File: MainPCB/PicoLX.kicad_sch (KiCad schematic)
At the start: 82 parts, among them J1 USB_C_Receptacle_USB2.0, J2 Conn_01x03, SW1 SW_Push, U1 RP2040, U2 W25Q32JVSS, U3 NCP1117-3.3_SOT223, U4 SN74LV1T34DBV, Y1 12.000MHz

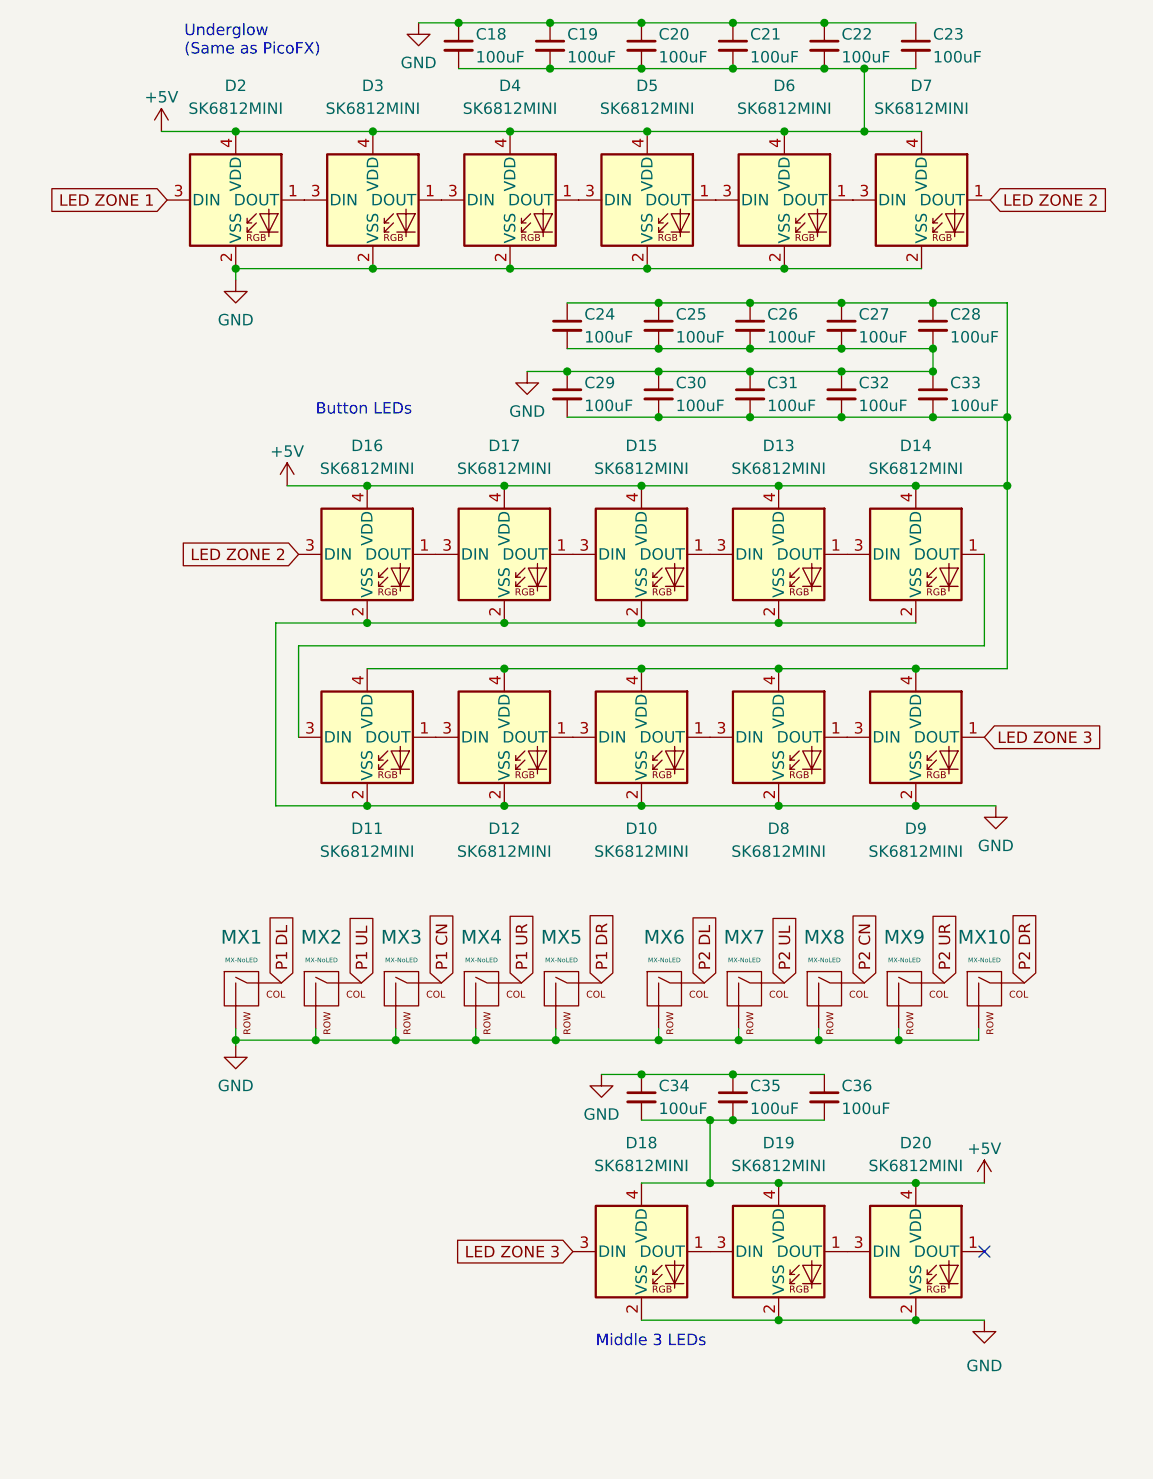
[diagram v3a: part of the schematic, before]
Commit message: fancy plate graphics, reroute all the LEDs because wrong pinout
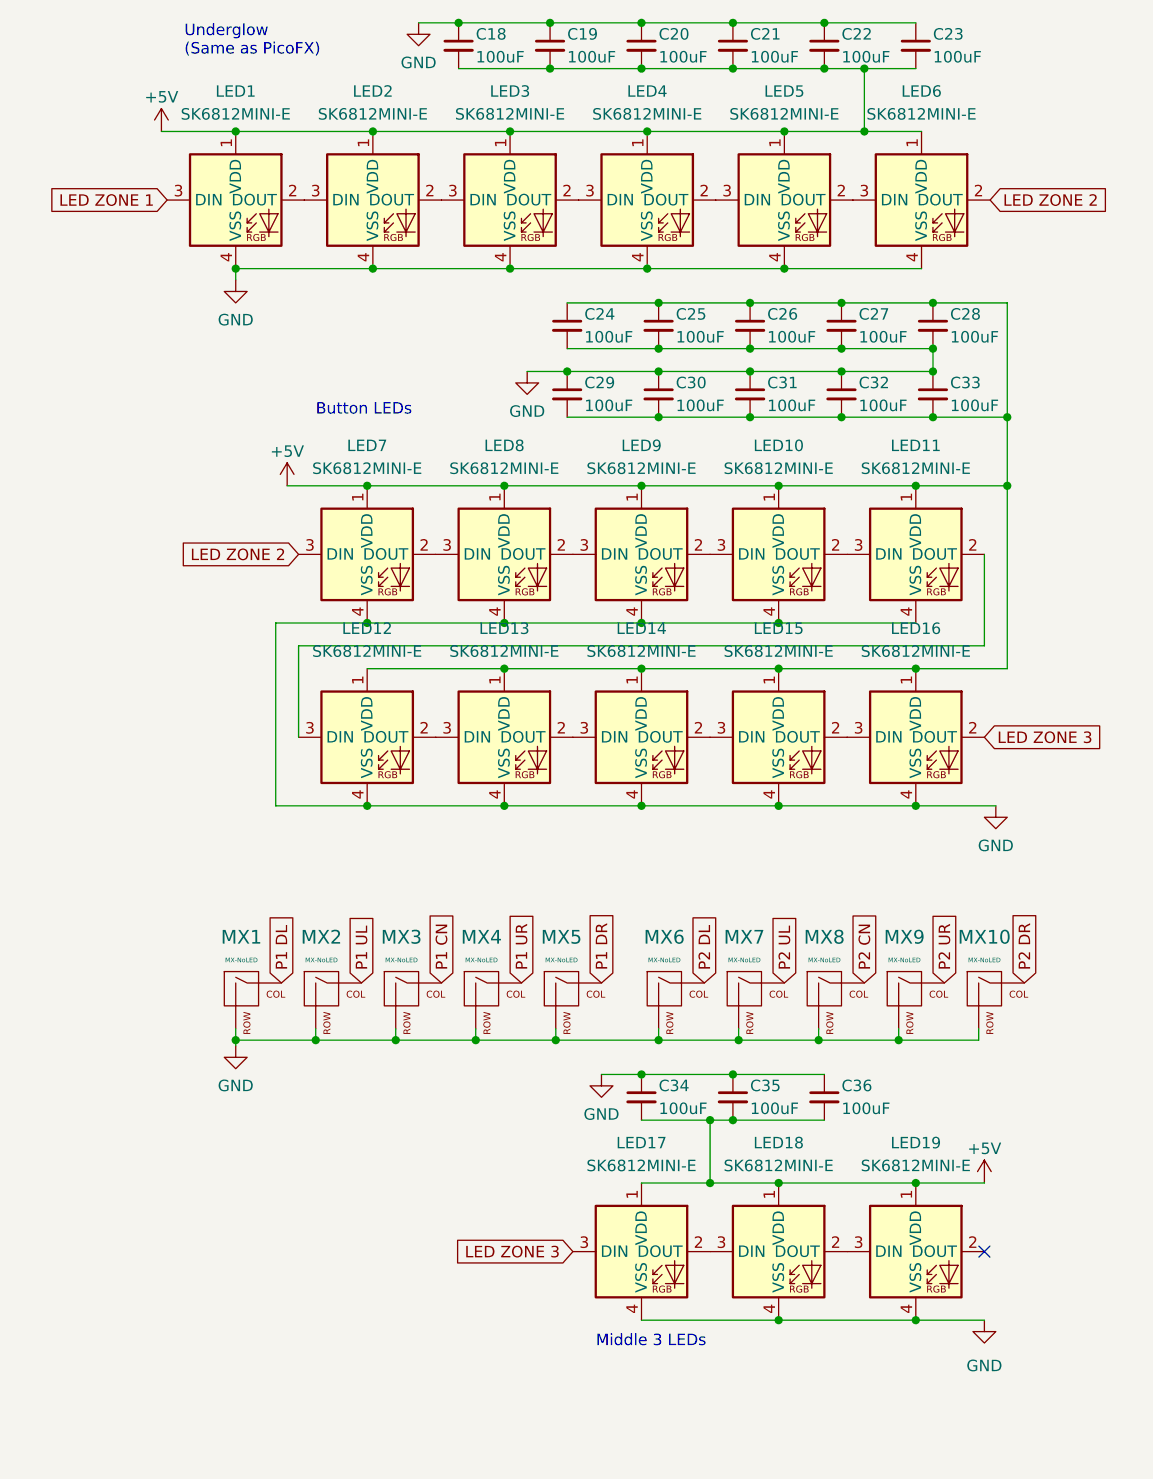
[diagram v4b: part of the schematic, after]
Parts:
- removed D10, D11, D12, D13, D14, D15, D16, D17, D18, D19, D2, D20, D3, D4, D5, D6, D7, D8, D9: SK6812MINI, marbastlib-various:LED_6028R, symbol LED:SK6812MINI
- added LED1, LED10, LED11, LED12, LED13, LED14, LED15, LED16, LED17, LED18, LED19, LED2, LED3, LED4, LED5, LED6, LED7, LED8, LED9: SK6812MINI-E, marbastlib-various:LED_6028R, symbol marbastlib-various:SK6812MINI-E
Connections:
- net +5V: now also LED1.1 (VDD), LED10.1 (VDD), LED11.1 (VDD), LED12.1 (VDD), LED13.1 (VDD), LED14.1 (VDD), LED15.1 (VDD), LED16.1 (VDD), LED17.1 (VDD), LED18.1 (VDD), LED19.1 (VDD), LED2.1 (VDD), LED3.1 (VDD), LED4.1 (VDD), LED5.1 (VDD), LED6.1 (VDD), LED7.1 (VDD), LED8.1 (VDD), LED9.1 (VDD)
- net GND: now also LED1.4 (VSS), LED10.4 (VSS), LED11.4 (VSS), LED12.4 (VSS), LED13.4 (VSS), LED14.4 (VSS), LED15.4 (VSS), LED16.4 (VSS), LED17.4 (VSS), LED18.4 (VSS), LED19.4 (VSS), LED2.4 (VSS), LED3.4 (VSS), LED4.4 (VSS), LED5.4 (VSS), LED6.4 (VSS), LED7.4 (VSS), LED8.4 (VSS), LED9.4 (VSS)
- net LED ZONE 1: now also LED1.3 (DIN)
- net LED ZONE 2: now also LED6.2 (DOUT), LED7.3 (DIN)
- net LED ZONE 3: now also LED16.2 (DOUT), LED17.3 (DIN)
- new net: LED5.2 (DOUT), LED6.3 (DIN)
- new net: LED11.2 (DOUT), LED12.3 (DIN)
- new net: LED10.2 (DOUT), LED11.3 (DIN)
- new net: LED18.2 (DOUT), LED19.3 (DIN)
- new net: LED4.2 (DOUT), LED5.3 (DIN)
- new net: LED15.2 (DOUT), LED16.3 (DIN)
- new net: LED14.2 (DOUT), LED15.3 (DIN)
- new net: LED2.2 (DOUT), LED3.3 (DIN)
- new net: LED1.2 (DOUT), LED2.3 (DIN)
- new net: LED17.2 (DOUT), LED18.3 (DIN)
- new net: LED13.2 (DOUT), LED14.3 (DIN)
- new net: LED3.2 (DOUT), LED4.3 (DIN)
- new net: LED7.2 (DOUT), LED8.3 (DIN)
- new net: LED10.3 (DIN), LED9.2 (DOUT)
- new net: LED8.2 (DOUT), LED9.3 (DIN)
- new net: LED12.2 (DOUT), LED13.3 (DIN)

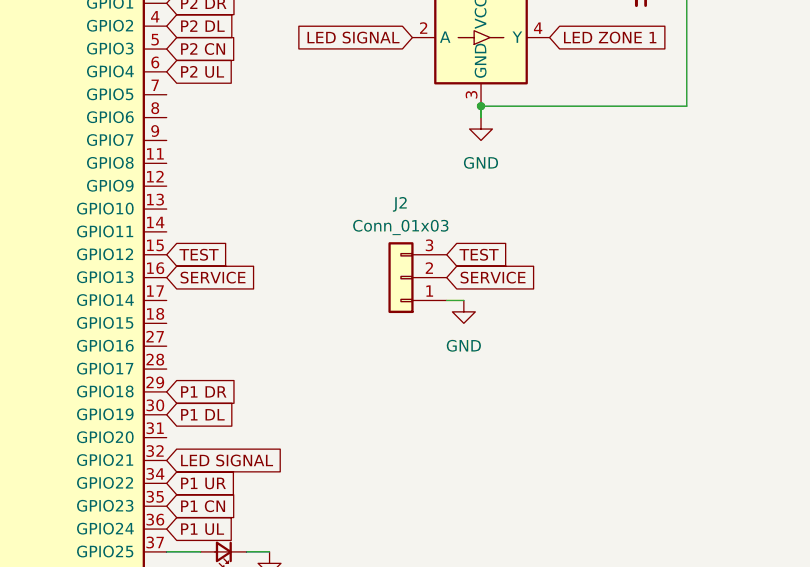
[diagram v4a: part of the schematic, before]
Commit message: Move buttons, add totally 100% real LEDs to plate
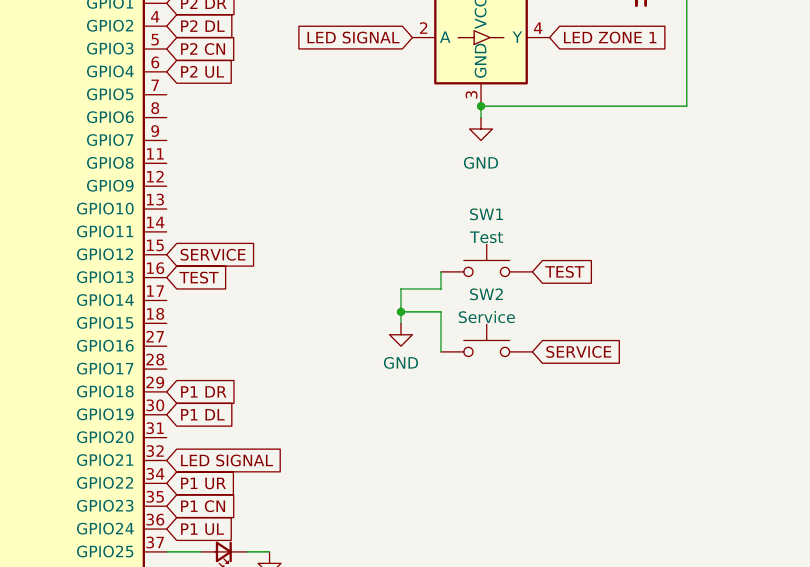
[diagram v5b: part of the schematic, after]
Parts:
- removed J2: Conn_01x03, Connector_PinHeader_2.54mm:PinHeader_1x03_P2.54mm_Vertical, symbol Connector_Generic:Conn_01x03
- added SW1: Test, Button_Switch_THT:SW_Tactile_SPST_Angled_PTS645Vx39-2LFS, symbol Switch:SW_Push
- added SW2: Service, Button_Switch_THT:SW_Tactile_SPST_Angled_PTS645Vx39-2LFS, symbol Switch:SW_Push
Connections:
- net GND: now also SW1.1, SW2.1
- net SERVICE: now also U1.15 (GPIO12), SW2.2; no longer U1.16 (GPIO13)
- net TEST: now also U1.16 (GPIO13), SW1.2; no longer U1.15 (GPIO12)
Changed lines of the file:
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@@
   (junction (at 243.205 50.165) (diameter 0) (color 0 0 0 0)
   )
+  (junction (at 118.11 96.52) (diameter 0) (color 0 0 0 0)
+  )
   (junction (at 109.22 41.91) (diameter 0) (color 0 0 0 0)
   )
@@
     (stroke (width 0) (type default))
   )
+  (wire (pts (xy 122.555 100.965) (xy 122.555 96.52))
+    (stroke (width 0) (type default))
+  )
   (wire (pts (xy 69.85 178.435) (xy 71.755 178.435))
     (stroke (width 0) (type default))
@@
     (stroke (width 0) (type default))
   )
+  (wire (pts (xy 122.555 93.98) (xy 122.555 92.075))
+    (stroke (width 0) (type default))
+  )
   (wire (pts (xy 238.76 135.89) (xy 238.76 142.875))
     (stroke (width 0) (type default))
@@
     (stroke (width 0) (type default))
   )
+  (wire (pts (xy 118.11 96.52) (xy 118.11 97.79))
+    (stroke (width 0) (type default))
+  )
   (wire (pts (xy 56.515 41.91) (xy 56.515 36.83))
     (stroke (width 0) (type default))
@@
     (stroke (width 0) (type default))
   )
+  (wire (pts (xy 118.11 93.98) (xy 118.11 96.52))
+    (stroke (width 0) (type default))
+  )
   (wire (pts (xy 201.295 41.275) (xy 216.535 41.275))
     (stroke (width 0) (type default))
@@
     (stroke (width 0) (type default))
   )
+  (wire (pts (xy 122.555 96.52) (xy 118.11 96.52))
+    (stroke (width 0) (type default))
+  )
   (wire (pts (xy 121.285 25.4) (xy 111.125 25.4))
     (stroke (width 0) (type default))
@@
     (stroke (width 0) (type default))
   )
-  (wire (pts (xy 123.19 95.25) (xy 125.095 95.25))
-    (stroke (width 0) (type default))
-  )
   (wire (pts (xy 76.835 20.32) (xy 80.645 20.32))
     (stroke (width 0) (type default))
@@
     (stroke (width 0) (type default))
   )
+  (wire (pts (xy 118.11 93.98) (xy 122.555 93.98))
+    (stroke (width 0) (type default))
+  )
   (wire (pts (xy 243.205 50.165) (xy 253.365 50.165))
     (stroke (width 0) (type default))
@@
     )
   )
-  (global_label "SERVICE" (shape input) (at 92.075 92.71 0) (fields_autoplaced)
+  (global_label "SERVICE" (shape input) (at 92.075 90.17 0) (fields_autoplaced)
     (effects (font (size 1.27 1.27)) (justify left))
-    (property "Intersheetrefs" "${INTERSHEET_REFS}" (at 102.7217 92.71 0)
+    (property "Intersheetrefs" "${INTERSHEET_REFS}" (at 102.7217 90.17 0)
       (effects (font (size 1.27 1.27)) (justify left) hide)
     )
@@
     )
   )
-  (global_label "TEST" (shape input) (at 92.075 90.17 0) (fields_autoplaced)
+  (global_label "TEST" (shape input) (at 92.075 92.71 0) (fields_autoplaced)
     (effects (font (size 1.27 1.27)) (justify left))
-    (property "Intersheetrefs" "${INTERSHEET_REFS}" (at 99.2745 90.17 0)
+    (property "Intersheetrefs" "${INTERSHEET_REFS}" (at 99.2745 92.71 0)
       (effects (font (size 1.27 1.27)) (justify left) hide)
     )
@@
     )
   )
-  (global_label "TEST" (shape input) (at 123.19 90.17 0) (fields_autoplaced)
+  (global_label "TEST" (shape input) (at 132.715 92.075 0) (fields_autoplaced)
     (effects (font (size 1.27 1.27)) (justify left))
-    (property "Intersheetrefs" "${INTERSHEET_REFS}" (at 130.3895 90.17 0)
+    (property "Intersheetrefs" "${INTERSHEET_REFS}" (at 139.9145 92.075 0)
       (effects (font (size 1.27 1.27)) (justify left) hide)
     )
@@
     )
   )
-  (global_label "SERVICE" (shape input) (at 123.19 92.71 0) (fields_autoplaced)
+  (global_label "SERVICE" (shape input) (at 132.715 100.965 0) (fields_autoplaced)
     (effects (font (size 1.27 1.27)) (justify left))
-    (property "Intersheetrefs" "${INTERSHEET_REFS}" (at 133.8367 92.71 0)
+    (property "Intersheetrefs" "${INTERSHEET_REFS}" (at 143.3617 100.965 0)
       (effects (font (size 1.27 1.27)) (justify left) hide)
     )
@@
     )
   )
-  (symbol (lib_id "Connector_Generic:Conn_01x03") (at 118.11 92.71 180) (unit 1)
-    (in_bom yes) (on_board yes) (dnp no) (fields_autoplaced)
-    (property "Reference" "J2" (at 118.11 84.455 0)
-      (effects (font (size 1.27 1.27)))
-    )
-    (property "Value" "Conn_01x03" (at 118.11 86.995 0)
-      (effects (font (size 1.27 1.27)))
-    )
-    (property "Footprint" "Connector_PinHeader_2.54mm:PinHeader_1x03_P2.54mm_Vertical" (at 118.11 92.71 0)
-      (effects (font (size 1.27 1.27)) hide)
-    )
-    (property "Datasheet" "~" (at 118.11 92.71 0)
-      (effects (font (size 1.27 1.27)) hide)
-    )
-    (pin "1")
-    (pin "2")
-    (pin "3")
-    (instances
-      (project "PicoLX"
-        (path "/c5e5d8b8-bebd-4318-85a6-adbafb95dd10"
-          (reference "J2") (unit 1)
-        )
-      )
-    )
-  )
   (symbol (lib_id "Device:C_Small") (at 251.46 16.51 0) (unit 1)
     (in_bom yes) (on_board yes) (dnp no)
@@
     )
   )
+  (symbol (lib_id "Switch:SW_Push") (at 127.635 92.075 0) (unit 1)
+    (in_bom yes) (on_board yes) (dnp no) (fields_autoplaced)
+    (property "Reference" "SW1" (at 127.635 85.725 0)
+      (effects (font (size 1.27 1.27)))
+    )
+    (property "Value" "Test" (at 127.635 88.265 0)
+      (effects (font (size 1.27 1.27)))
+    )
+    (property "Footprint" "Button_Switch_THT:SW_Tactile_SPST_Angled_PTS645Vx39-2LFS" (at 127.635 86.995 0)
+      (effects (font (size 1.27 1.27)) hide)
+    )
+    (property "Datasheet" "~" (at 127.635 86.995 0)
+      (effects (font (size 1.27 1.27)) hide)
+    )
+    (pin "1")
+    (pin "2")
+    (instances
+      (project "MainPlate"
+        (path "/99dc8099-532a-4f61-b2bb-5f32226d143c"
+          (reference "SW1") (unit 1)
+        )
+      )
+      (project "PicoLX"
+        (path "/c5e5d8b8-bebd-4318-85a6-adbafb95dd10"
+          (reference "SW2") (unit 1)
+        )
+      )
+    )
+  )
   (symbol (lib_id "marbastlib-various:SK6812MINI-E") (at 201.295 33.655 0) (unit 1)
     (in_bom yes) (on_board yes) (dnp no)
@@
     )
   )
-  (symbol (lib_id "power:GND") (at 125.095 95.25 0) (unit 1)
-    (in_bom yes) (on_board yes) (dnp no) (fields_autoplaced)
-    (property "Reference" "#PWR034" (at 125.095 101.6 0)
-      (effects (font (size 1.27 1.27)) hide)
-    )
-    (property "Value" "GND" (at 125.095 100.33 0)
-      (effects (font (size 1.27 1.27)))
-    )
-    (property "Footprint" "" (at 125.095 95.25 0)
-      (effects (font (size 1.27 1.27)) hide)
-    )
-    (property "Datasheet" "" (at 125.095 95.25 0)
-      (effects (font (size 1.27 1.27)) hide)
-    )
-    (pin "1")
-    (instances
-      (project "PicoLX"
-        (path "/c5e5d8b8-bebd-4318-85a6-adbafb95dd10"
-          (reference "#PWR034") (unit 1)
-        )
-      )
-      (project "Panel"
-        (path "/f55927e3-6490-4e79-9229-dceeb24f0064"
-          (reference "#PWR015") (unit 1)
-        )
-      )
-    )
-  )
   (symbol (lib_name "GND_1") (lib_id "power:GND") (at 186.055 42.545 0) (unit 1)
     (in_bom yes) (on_board yes) (dnp no) (fields_autoplaced)
@@
     )
   )
+  (symbol (lib_id "Switch:SW_Push") (at 127.635 100.965 0) (unit 1)
+    (in_bom yes) (on_board yes) (dnp no) (fields_autoplaced)
+    (property "Reference" "SW2" (at 127.635 94.615 0)
+      (effects (font (size 1.27 1.27)))
+    )
+    (property "Value" "Service" (at 127.635 97.155 0)
+      (effects (font (size 1.27 1.27)))
+    )
+    (property "Footprint" "Button_Switch_THT:SW_Tactile_SPST_Angled_PTS645Vx39-2LFS" (at 127.635 95.885 0)
+      (effects (font (size 1.27 1.27)) hide)
+    )
+    (property "Datasheet" "~" (at 127.635 95.885 0)
+      (effects (font (size 1.27 1.27)) hide)
+    )
+    (pin "1")
+    (pin "2")
+    (instances
+      (project "MainPlate"
+        (path "/99dc8099-532a-4f61-b2bb-5f32226d143c"
+          (reference "SW2") (unit 1)
+        )
+      )
+      (project "PicoLX"
+        (path "/c5e5d8b8-bebd-4318-85a6-adbafb95dd10"
+          (reference "SW3") (unit 1)
+        )
+      )
+    )
+  )
   (symbol (lib_id "marbastlib-various:SK6812MINI-E") (at 216.535 33.655 0) (unit 1)
     (in_bom yes) (on_board yes) (dnp no)
@@
         )
       )
+    )
+  )
+  (symbol (lib_id "power:GND") (at 118.11 97.79 0) (unit 1)
+    (in_bom yes) (on_board yes) (dnp no) (fields_autoplaced)
+    (property "Reference" "#PWR01" (at 118.11 104.14 0)
+      (effects (font (size 1.27 1.27)) hide)
+    )
+    (property "Value" "GND" (at 118.11 102.235 0)
+      (effects (font (size 1.27 1.27)))
+    )
+    (property "Footprint" "" (at 118.11 97.79 0)
+      (effects (font (size 1.27 1.27)) hide)
+    )
+    (property "Datasheet" "" (at 118.11 97.79 0)
+      (effects (font (size 1.27 1.27)) hide)
+    )
+    (pin "1")
+    (instances
+      (project "MainPlate"
+        (path "/99dc8099-532a-4f61-b2bb-5f32226d143c"
+          (reference "#PWR01") (unit 1)
+        )
+      )
+      (project "PicoLX"
+        (path "/c5e5d8b8-bebd-4318-85a6-adbafb95dd10"
+          (reference "#PWR035") (unit 1)
+        )
+      )

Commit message: Update README, generate gerbers, minor fixes
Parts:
- removed F1: 500mA, Fuse:Fuse_1206_3216Metric_Pad1.42x1.75mm_HandSolder, symbol Device:Fuse_Small
- added R2: DNF, Resistor_SMD:R_0402_1005Metric_Pad0.72x0.64mm_HandSolder, symbol Device:R_Small
- C17: LCSC (none) -> C1525
- C18, C19, C20, C21, C22, C23, C24, C25, C26, C27, C28, C29, C30, C31, C32, C33, C34, C35, C36: footprint Capacitor_SMD:C_0402_1005Metric_Pad0.74x0.62mm_HandSolder -> Capacitor_SMD:C_0805_2012Metric_Pad1.18x1.45mm_HandSolder; LCSC (none) -> C15008
- C3, C6: LCSC C29266 -> C52923
- D1: value LED_Small -> DNF
- J1: LCSC (none) -> C2988369
- SW1: LCSC (none) -> C318884
- U4: LCSC (none) -> C100024
- Y1: LCSC (none) -> C9002
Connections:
- net +5V: now also J1.A4 (VBUS), J1.A9 (VBUS), J1.B4 (VBUS), J1.B9 (VBUS)
- net at U1.37 (GPIO25): now also R2.1; no longer D1.2 (A)
- new net: D1.2 (A), R2.2
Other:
- moved on the sheet: D1
